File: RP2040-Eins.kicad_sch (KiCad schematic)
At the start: 45 parts, among them J1 CONN_L, J2 CONN_U, J3 CONN_R2, J4 CONN_R, J5 CONN_R3, J6 USB_B_Micro, J7 CONN_JTAG, Q1 AO3400A, U1 W25Q128JVS, U2 RP2040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

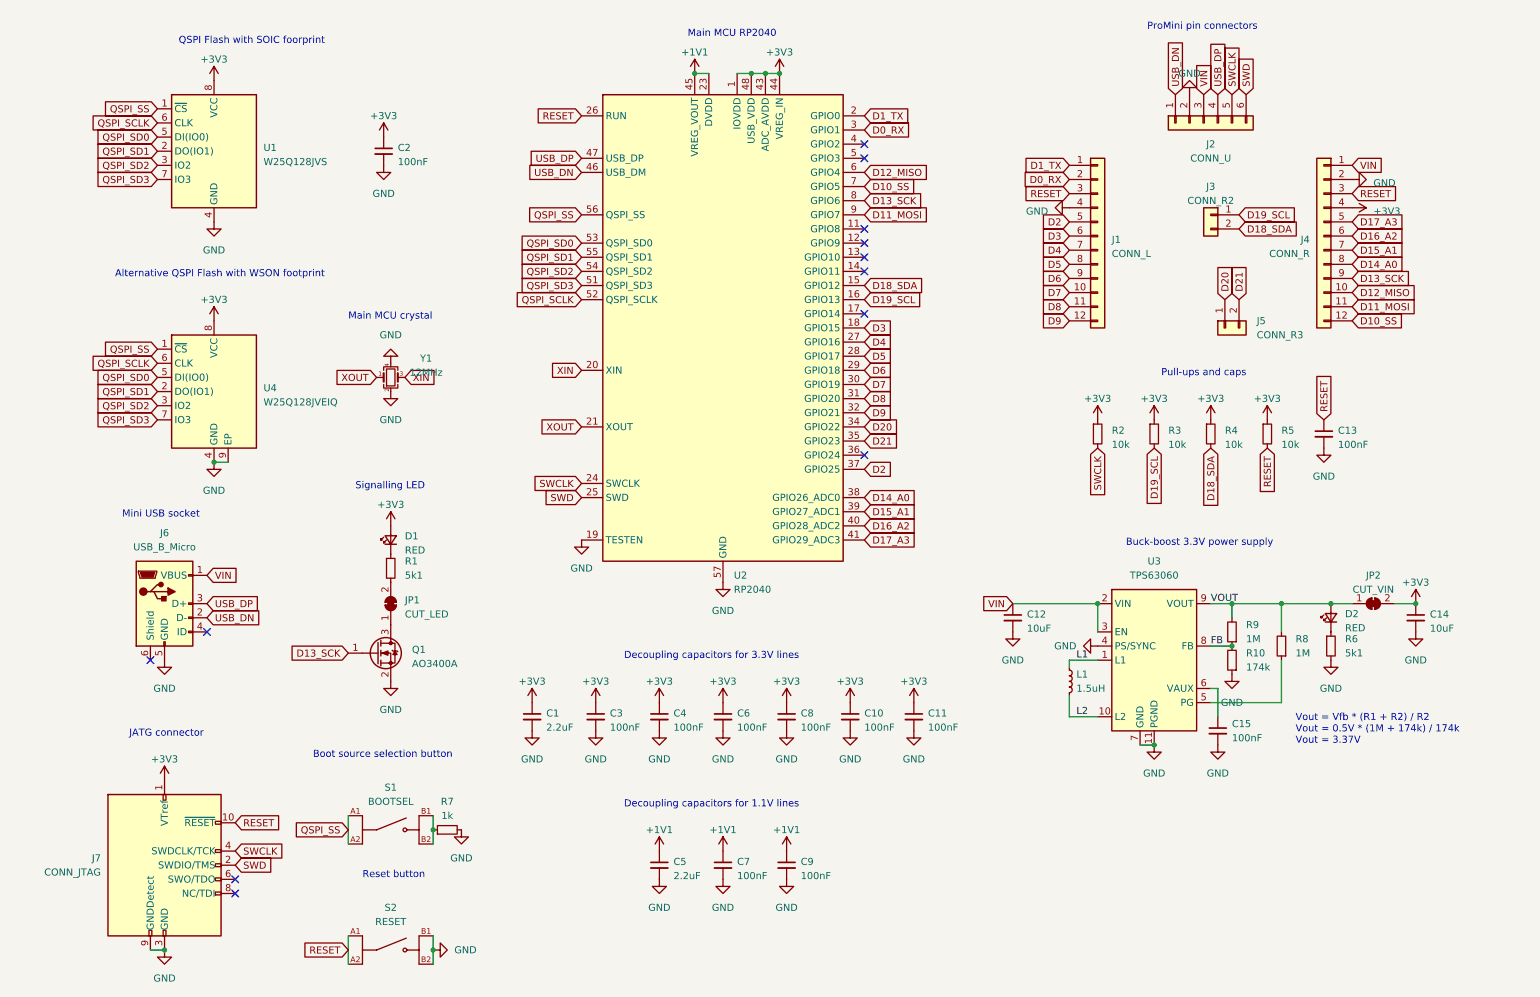
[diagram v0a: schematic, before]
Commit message: Added LDO power and UNO pinout
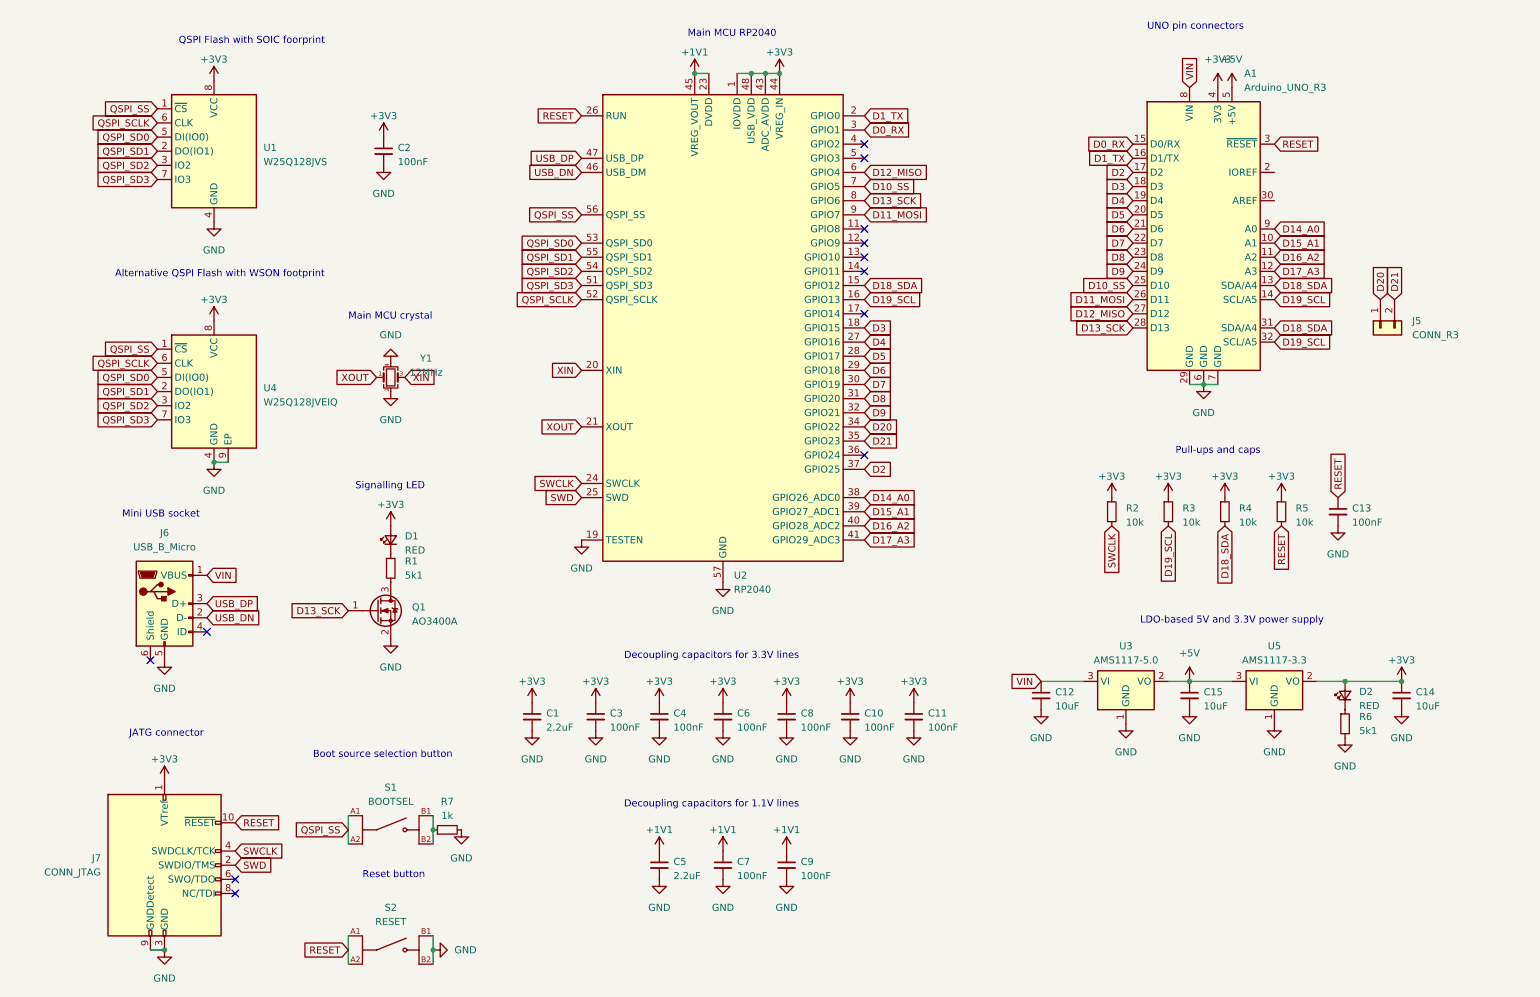
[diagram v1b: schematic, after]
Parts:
- removed J1: CONN_L, Connector_PinHeader_2.54mm:PinHeader_1x12_P2.54mm_Vertical, symbol Connector_Generic:Conn_01x12
- removed J2: CONN_U, Connector_PinHeader_2.54mm:PinHeader_1x06_P2.54mm_Vertical, symbol Connector_Generic:Conn_01x06
- removed J3: CONN_R2, Connector_PinHeader_2.54mm:PinHeader_1x02_P2.54mm_Vertical, symbol Connector_Generic:Conn_01x02
- removed J4: CONN_R, Connector_PinHeader_2.54mm:PinHeader_1x12_P2.54mm_Vertical, symbol Connector_Generic:Conn_01x12
- removed JP1: CUT_LED, Jumper:SolderJumper-2_P1.3mm_Bridged_RoundedPad1.0x1.5mm, symbol Jumper:SolderJumper_2_Bridged
- removed JP2: CUT_VIN, Jumper:SolderJumper-2_P1.3mm_Bridged_RoundedPad1.0x1.5mm, symbol Jumper:SolderJumper_2_Bridged
- removed L1: 1.5uH, Inductor_SMD:L_Murata_DFE201610P, symbol Device:L_Small
- removed R10: 174k, Resistor_SMD:R_0402_1005Metric, symbol Device:R_Small
- removed R8, R9: 1M, Resistor_SMD:R_0402_1005Metric, symbol Device:R_Small
- removed U3: TPS63060, Package_SON:Texas_S-PWSON-N10_ThermalVias, symbol Regulator_Switching:TPS63060
- added A1: Arduino_UNO_R3, Module:Arduino_UNO_R3_WithMountingHoles, symbol MCU_Module:Arduino_UNO_R3
- added U3: AMS1117-5.0, Package_TO_SOT_SMD:SOT-223-3_TabPin2, symbol Regulator_Linear:AMS1117-5.0
- added U5: AMS1117-3.3, Package_TO_SOT_SMD:SOT-223-3_TabPin2, symbol Regulator_Linear:AMS1117-3.3
- C15: value 100nF -> 10uF; footprint Capacitor_SMD:C_0402_1005Metric -> Capacitor_SMD:C_0805_2012Metric
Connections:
- net VOUT is gone; now on net +3V3: D2.2 (A)
- net +3V3: now also A1.4 (3V3), U5.2 (VO)
- net D0_RX: now also A1.15 (D0/RX)
- net D10_SS: now also A1.25 (D10)
- net D11_MOSI: now also A1.26 (D11)
- net D12_MISO: now also A1.27 (D12)
- net D13_SCK: now also A1.28 (D13)
- net D14_A0: now also A1.9 (A0)
- net D15_A1: now also A1.10 (A1)
- net D16_A2: now also A1.11 (A2)
- net D17_A3: now also A1.12 (A3)
- net D18_SDA: now also A1.13 (SDA/A4), A1.31 (SDA/A4)
- net D19_SCL: now also A1.14 (SCL/A5), A1.32 (SCL/A5)
- net D1_TX: now also A1.16 (D1/TX)
- net D2: now also A1.17 (D2)
- net D3: now also A1.18 (D3)
- net D4: now also A1.19 (D4)
- net D5: now also A1.20 (D5)
- net D6: now also A1.21 (D6)
- net D7: now also A1.22 (D7)
- net D8: now also A1.23 (D8)
- net D9: now also A1.24 (D9)
- net GND: now also A1.29 (GND), A1.6 (GND), A1.7 (GND), U3.1 (GND), U5.1 (GND)
- net RESET: now also A1.3 (~{RESET})
- net VIN: now also A1.8 (VIN), U3.3 (VI)
- net at R1.2: now also Q1.3 (D)
- net +5V: now reaches C15.1
- net +5V: now also A1.5 (+5V), U3.2 (VO), U5.3 (VI)
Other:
- note added: "LDO-based 5V and 3.3V power supply"
- note added: "UNO pin connectors"
- note removed: "Buck-boost 3.3V power supply"
- note removed: "ProMini pin connectors"
- note removed: "Vout = Vfb * (R1 + R2) / R2 Vout = 0.5V * (1M + 174k) / 174k Vout = 3.37V"
- title: RP2040-ProMini-0030 -> RP2040-Eins-0010
- moved on the sheet: C12, C13, C14, D2, J5, Q1, R2, R3, R4, R5, R6

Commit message: Added few components
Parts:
- added C16: 2.2uF, Capacitor_SMD:C_0603_1608Metric, symbol Device:C_Small
- added J1: Barrel_Jack_Switch, Connector_BarrelJack:BarrelJack_Horizontal, symbol Connector:Barrel_Jack_Switch
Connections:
- net +3V3: now also C16.1
- net GND: now also C16.2, J1.2, J1.3
- net VIN: now also J1.1; no longer J6.1 (VBUS)
- new net VBUS: J6.1 (VBUS)
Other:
- note added: "Power jack"
- moved on the sheet: A1, C12, C13, C14, C15, C2, D2, J5, R2, R3, R4, R5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

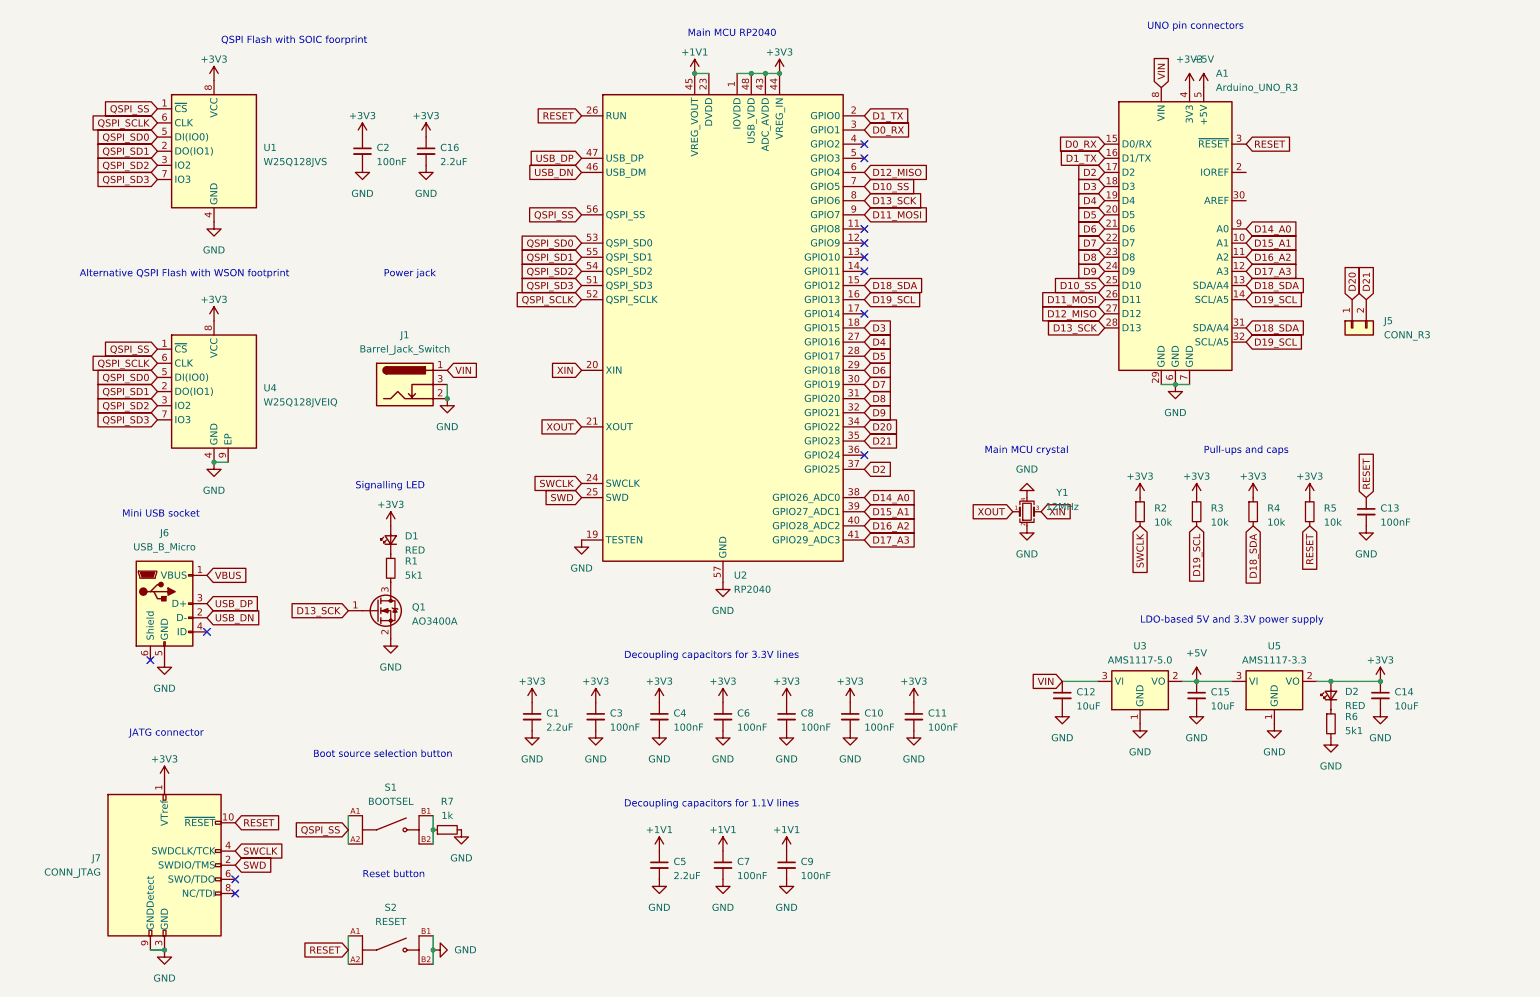
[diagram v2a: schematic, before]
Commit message: Added more components to schematics
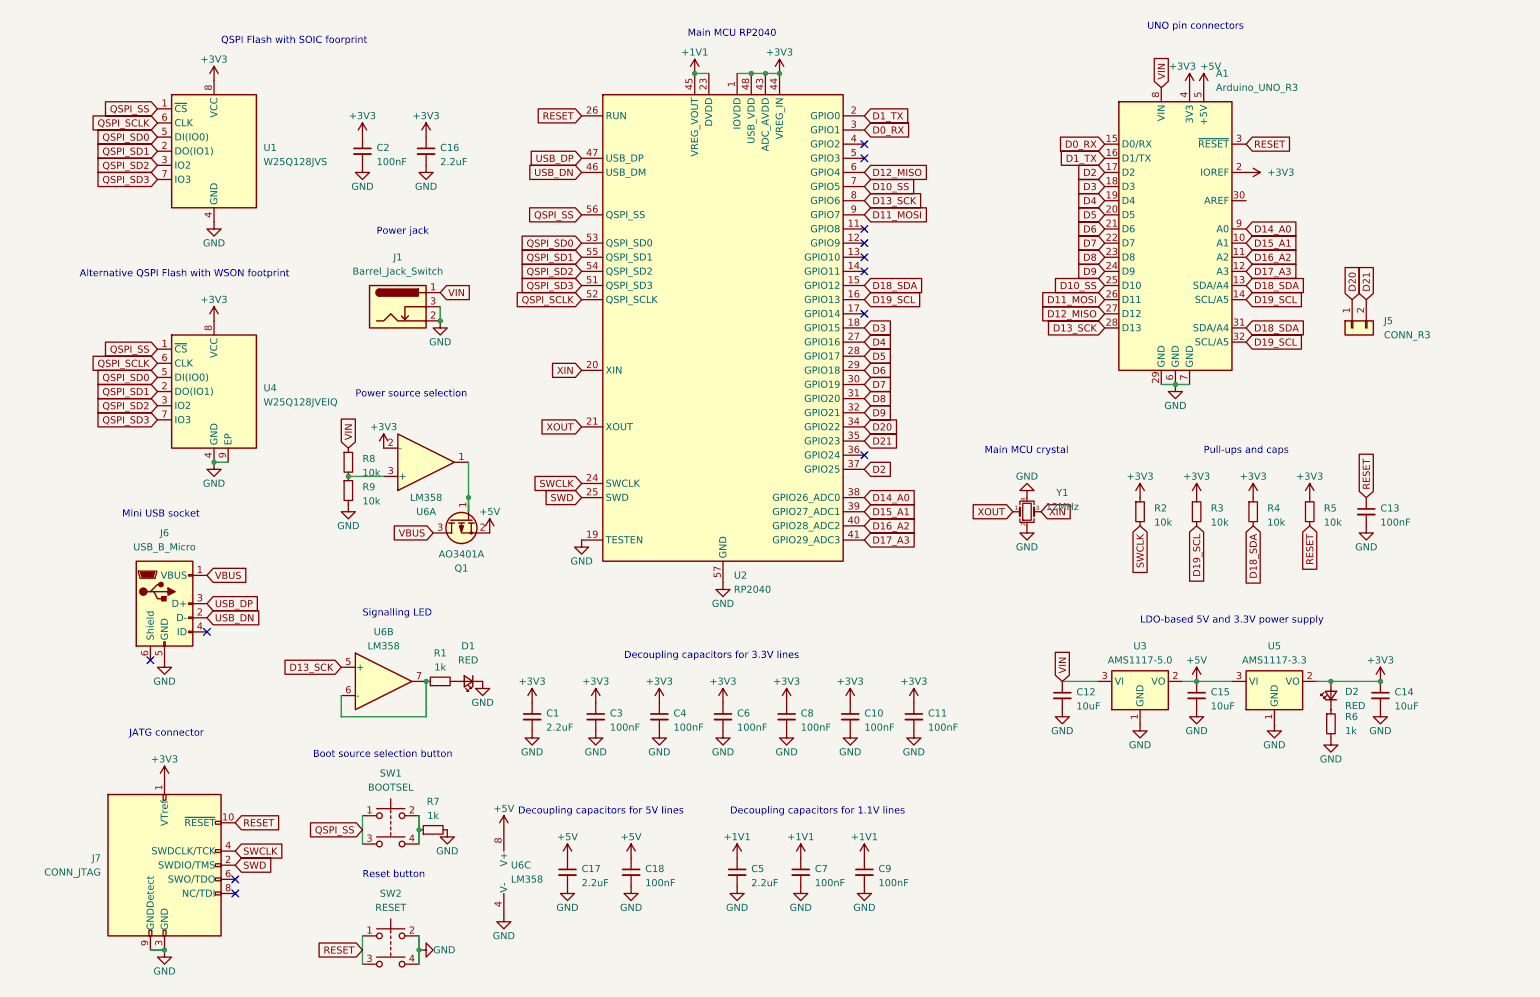
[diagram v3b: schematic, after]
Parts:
- removed Q1: AO3400A, Package_TO_SOT_SMD:SOT-23, symbol Transistor_FET:AO3400A
- removed S1: BOOTSEL, RP2040-ProMini:SW_EVPBB0AAB000, symbol EVPBB0AAB000:EVPBB0AAB000
- removed S2: RESET, RP2040-ProMini:SW_EVPBB0AAB000, symbol EVPBB0AAB000:EVPBB0AAB000
- added C17: 2.2uF, Capacitor_SMD:C_0603_1608Metric, symbol Device:C_Small
- added C18: 100nF, Capacitor_SMD:C_0402_1005Metric, symbol Device:C_Small
- added Q1: AO3401A, Package_TO_SOT_SMD:SOT-23, symbol PCM_Transistor_MOSFET_AKL:AO3401A
- added R8, R9: 10k, Resistor_SMD:R_0402_1005Metric, symbol Device:R_Small
- added SW1: BOOTSEL, PCM_4ms_Switch:Button_Tact_Sqkg, symbol Switch:SW_Push_Dual
- added SW2: RESET, PCM_4ms_Switch:Button_Tact_Sqkg, symbol Switch:SW_Push_Dual
- added U6: LM358, Package_SO:SOIC-8_3.9x4.9mm_P1.27mm, symbol Amplifier_Operational:LM358
- R1, R6: value 5k1 -> 1k
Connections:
- net +3V3: now also A1.2 (IOREF), U6.2 (-); no longer D1.2 (A)
- net +5V: now also C17.1, C18.1, Q1.2 (S), U6.8 (V+)
- net D13_SCK: now also U6.5 (+)
- net GND: now also D1.1 (K), C17.2, C18.2, R9.2, SW2.2, SW2.4, U6.4 (V-)
- net QSPI_SS: now also SW1.1, SW1.3
- net RESET: now also SW2.1, SW2.3
- net VBUS: now also Q1.3 (D)
- net VIN: now also R8.1
- net at R7.1: now also SW1.2, SW1.4
- net at R1.1: now also U6.6 (-), U6.7; no longer D1.1 (K)
- net at R1.2: now also D1.2 (A)
- new net: R8.2, R9.1, U6.3 (+)
- new net: Q1.1 (G), U6.1
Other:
- note added: "Decoupling capacitors for 5V lines"
- note added: "Power source selection"
- moved on the sheet: C5, C7, C9, D1, J1, R1, R7
